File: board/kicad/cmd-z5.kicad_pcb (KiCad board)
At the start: 2 copper layers, 43.2 x 82.4 mm, 92 parts, among them J1 USB4105-GF-A, J2 Battery 1S Li-ion, J3 SWD, J4 TBS M10N, J5 X05A20H26G, J6 FH12-28S-0.5SH(55), Q1 DMG1024UV, Q2 DMG1016UDW, U1 USBLC6-2SC6, U2 nPM1300-QEAA-R7, U3 nRF52840-QIAA-R, U4 LIS2DH12TR, U5 Wio-SX1262, U6 TPS610997YFFR, U7 PAM8302AASCR, Y1 32 MHz CL=10pF, Y2 32.768 kHz CL=7pF

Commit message: Replaced FFC connectors with low profile ones
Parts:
- J5: footprint Connector_FFC-FPC:Hirose_FH12-26S-0.5SH_1x26-1MP_P0.50mm_Horizontal -> cmd-z5:FPC-SMD_26P-P0.50_X05A20H26G
- J6: footprint Connector_FFC-FPC:Hirose_FH12-28S-0.5SH_1x28-1MP_P0.50mm_Horizontal -> cmd-z5:FPC-SMD_28P-P0.50_FH12-28S-0.5SH-55
- moved J5 0.55 mm to (109.1, 70.4)
- moved J6 0.36 mm to (91.7, 80.9)

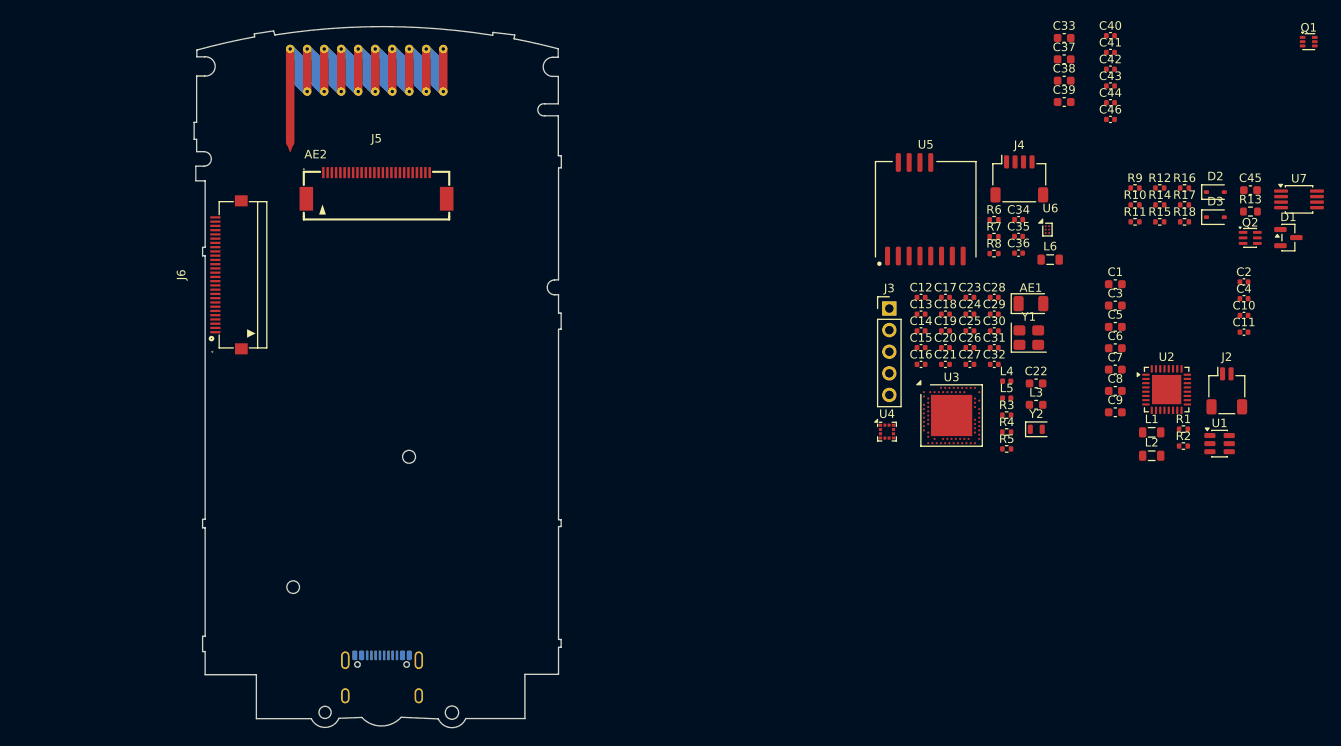
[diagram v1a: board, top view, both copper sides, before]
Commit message: Added microphone and battery contacts
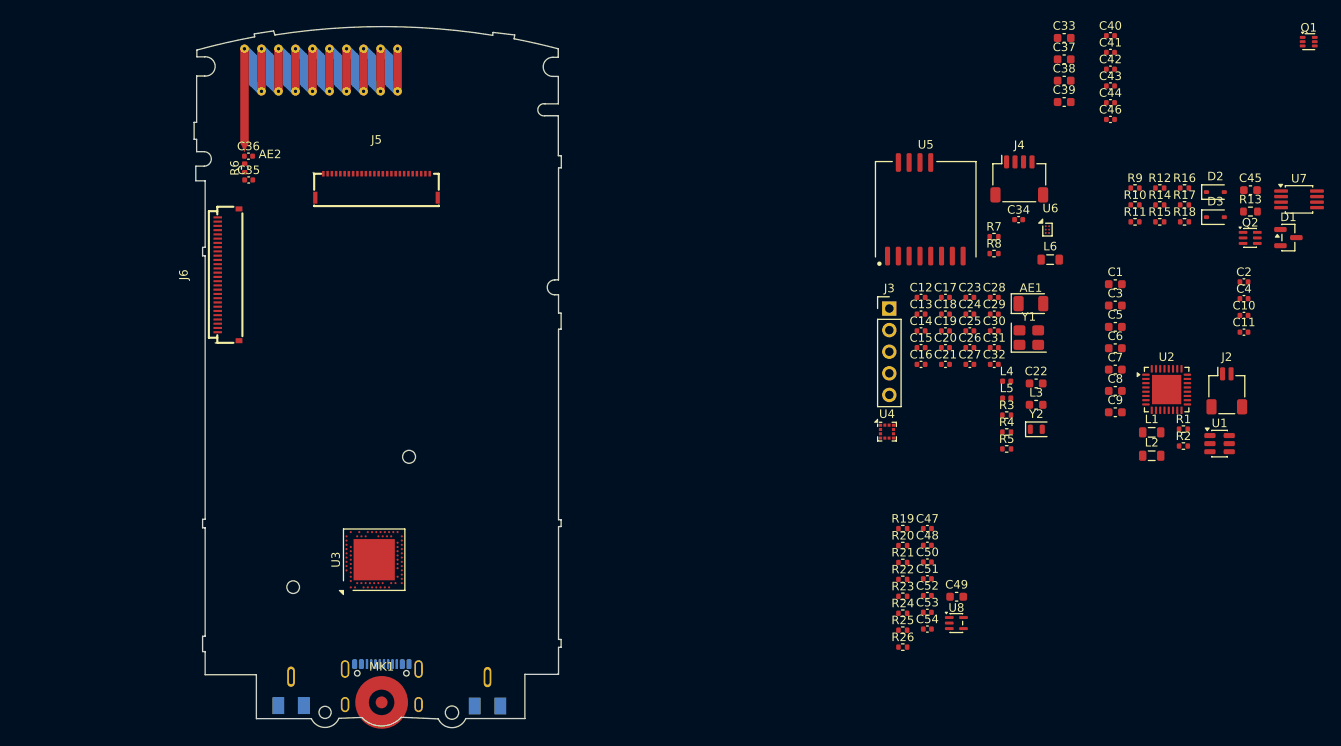
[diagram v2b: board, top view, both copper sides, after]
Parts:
- added C47: 1u, Capacitor_SMD:C_0402_1005Metric, F.Cu at (173.8, 110.7)
- added C48: 330p, Capacitor_SMD:C_0402_1005Metric, F.Cu at (173.8, 112.7)
- added C49: 10u, Capacitor_SMD:C_0603_1608Metric, F.Cu at (177.3, 118.7)
- added C50: 1u, Capacitor_SMD:C_0402_1005Metric, F.Cu at (173.8, 114.7)
- added C51: 4.7u, Capacitor_SMD:C_0402_1005Metric, F.Cu at (173.8, 116.6)
- added C52: 1u, Capacitor_SMD:C_0402_1005Metric, F.Cu at (173.8, 118.6)
- added C53: 100n, Capacitor_SMD:C_0402_1005Metric, F.Cu at (173.8, 120.6)
- added C54: 10n, Capacitor_SMD:C_0402_1005Metric, F.Cu at (173.8, 122.5)
- added J2: GT-BTP30002-0500B-015A, cmd-z5:BAT-SMD_2P-P3.00_G-Switch_GT-BTP30002-0500B-015A, B.Cu at (122.1, 129.0)
- added J7: GT-BTP30002-0500B-015A, cmd-z5:BAT-SMD_2P-P3.00_G-Switch_GT-BTP30002-0500B-015A, B.Cu at (99.0, 129.0)
- added MK1: Capsule mic (original), cmd-z5:MIC_Contact_Concentric_D6.2mm, F.Cu at (109.7, 131.2)
- added R19: 1k, Resistor_SMD:R_0402_1005Metric, F.Cu at (171.0, 110.7)
- added R20: 2.2k, Resistor_SMD:R_0402_1005Metric, F.Cu at (171.0, 112.7)
- added R21: 100k, Resistor_SMD:R_0402_1005Metric, F.Cu at (171.0, 114.7)
- added R22: 100k, Resistor_SMD:R_0402_1005Metric, F.Cu at (171.0, 116.7)
- added R23: 100k, Resistor_SMD:R_0402_1005Metric, F.Cu at (171.0, 118.7)
- added R24: 2.2k, Resistor_SMD:R_0402_1005Metric, F.Cu at (171.0, 120.7)
- added R25: 1k, Resistor_SMD:R_0402_1005Metric, F.Cu at (171.0, 122.7)
- added R26: 100k, Resistor_SMD:R_0402_1005Metric, F.Cu at (171.0, 124.7)
- added U8: TLV9001IDCKR, Package_TO_SOT_SMD:SOT-353_SC-70-5, F.Cu at (177.3, 121.8)
- J5: value X05A20H26G -> KH-FPC0.5-H1.0SMT-26P-QCHF; footprint cmd-z5:FPC-SMD_26P-P0.50_X05A20H26G -> cmd-z5:FPC-SMD_26P-P0.50_KH-FPC0.5-H1.0SMT-26P-QCHF
- J6: value FH12-28S-0.5SH(55) -> KH-FPC0.5-H1.0SMT-28P-QCHF; footprint cmd-z5:FPC-SMD_28P-P0.50_FH12-28S-0.5SH-55 -> cmd-z5:FPC-SMD_28P-P0.50_KH-FPC0.5-H1.0SMT-28P-QCHF
- moved C36 91.3 mm to (94.0, 66.9)
- moved C35 90.8 mm to (94.0, 69.7)
- moved R6 88.3 mm to (93.6, 68.3), turned to 90 degrees
- moved U3 70.0 mm to (108.8, 114.4), turned to 90 degrees
- moved AE2 5.38 mm to (102.5, 60.1)
- moved J1 1.03 mm to (109.7, 130.3)
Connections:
- U2 pad 8: unconnected-(U2-GPIO1-Pad8) -> MIC_VDD
- U3 pad K2: unconnected-(U3-AIN3/P0.05-PadK2) -> /MCU/MIC_OUT

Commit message: Fixed component positions
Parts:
- removed the J2 at (209.1, 94.5)
- added D4: green, LED_SMD:LED_0603_1608Metric, F.Cu at (98.0, 66.8)
- added D5: green, LED_SMD:LED_0603_1608Metric, F.Cu at (106.0, 67.0)
- added D6: green, LED_SMD:LED_0603_1608Metric, F.Cu at (113.7, 66.9)
- added D7: green, LED_SMD:LED_0603_1608Metric, F.Cu at (121.7, 66.8)
- added J8: Battery header, Connector_PinHeader_2.54mm:PinHeader_1x02_P2.54mm_Vertical, F.Cu at (123.3, 123.4)
- added R27: 330, Resistor_SMD:R_0402_1005Metric, F.Cu at (68.6, 94.2)
- added R28: 330, Resistor_SMD:R_0402_1005Metric, F.Cu at (68.6, 96.2)
- added R29: 330, Resistor_SMD:R_0402_1005Metric, F.Cu at (68.6, 98.2)
- added R30: 330, Resistor_SMD:R_0402_1005Metric, F.Cu at (68.6, 100.2)
- U5: moved to B.Cu
- moved U5 78.3 mm to (95.5, 77.3), turned to 180 degrees
- moved U3 77.7 mm to (164.7, 60.5)

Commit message: Few physical modifications
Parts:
- AE1, C12, C13, C14, C15, C16, C17, C18, C19, C20, C21, C22, C23, C24, C25, C26, C27, C28, C29, C30, C33, C34, C40, C41, C42, C43, C44, C45, C46, D1, D2, D3, L3, L4, L5, Q1, Q2, R10, R11, R12, R13, R14, R15, R16, R17, R18, R27, R28, R29, R3, R30, R9, U1, U3, U7, Y1, Y2: moved to B.Cu
- AE2: footprint RF_Antenna:Texas_SWRA416_868MHz_915MHz -> cmd-z5:Texas_SWRA416_868MHz_915MHz_Mirrored
- J4: footprint Connector_JST:JST_SH_SM04B-SRSS-TB_1x04-1MP_P1.00mm_Horizontal -> cmd-z5:SolderPads_1x04_P2.00mm_SMD; moved to B.Cu
- moved Q1 116.6 mm to (118.0, 112.3)
- moved C4 115.3 mm to (99.8, 114.0)
- moved D1 110.8 mm to (109.4, 105.8), turned to 180 degrees
- moved C45 109.6 mm to (109.2, 109.3), turned to 180 degrees
- moved C11 108.8 mm to (103.7, 104.8), turned to 90 degrees
- moved C10 108.0 mm to (104.8, 104.8), turned to 90 degrees
- moved C2 105.2 mm to (109.1, 107.8)
- moved R13 103.1 mm to (115.3, 109.8)
- moved R10 103.0 mm to (95.3, 70.5), turned to 180 degrees
- moved U7 102.4 mm to (120.5, 104.8), turned to 90 degrees
- moved R11 100.8 mm to (97.6, 70.5)
- moved L2 100.6 mm to (100.0, 111.2), turned to 180 degrees
- moved U1 100.5 mm to (110.2, 123.0), turned to -90 degrees
- moved D2 99.9 mm to (114.5, 107.0), turned to -90 degrees
- moved C5 99.6 mm to (98.6, 108.0), turned to 180 degrees
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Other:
- board size 43.2 x 82.4 mm -> 43 x 82.4 mm
